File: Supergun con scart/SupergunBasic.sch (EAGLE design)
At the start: 37 parts, among them J1 AUDIO_JACK_3.5MM_PTH, X2 SCART-F

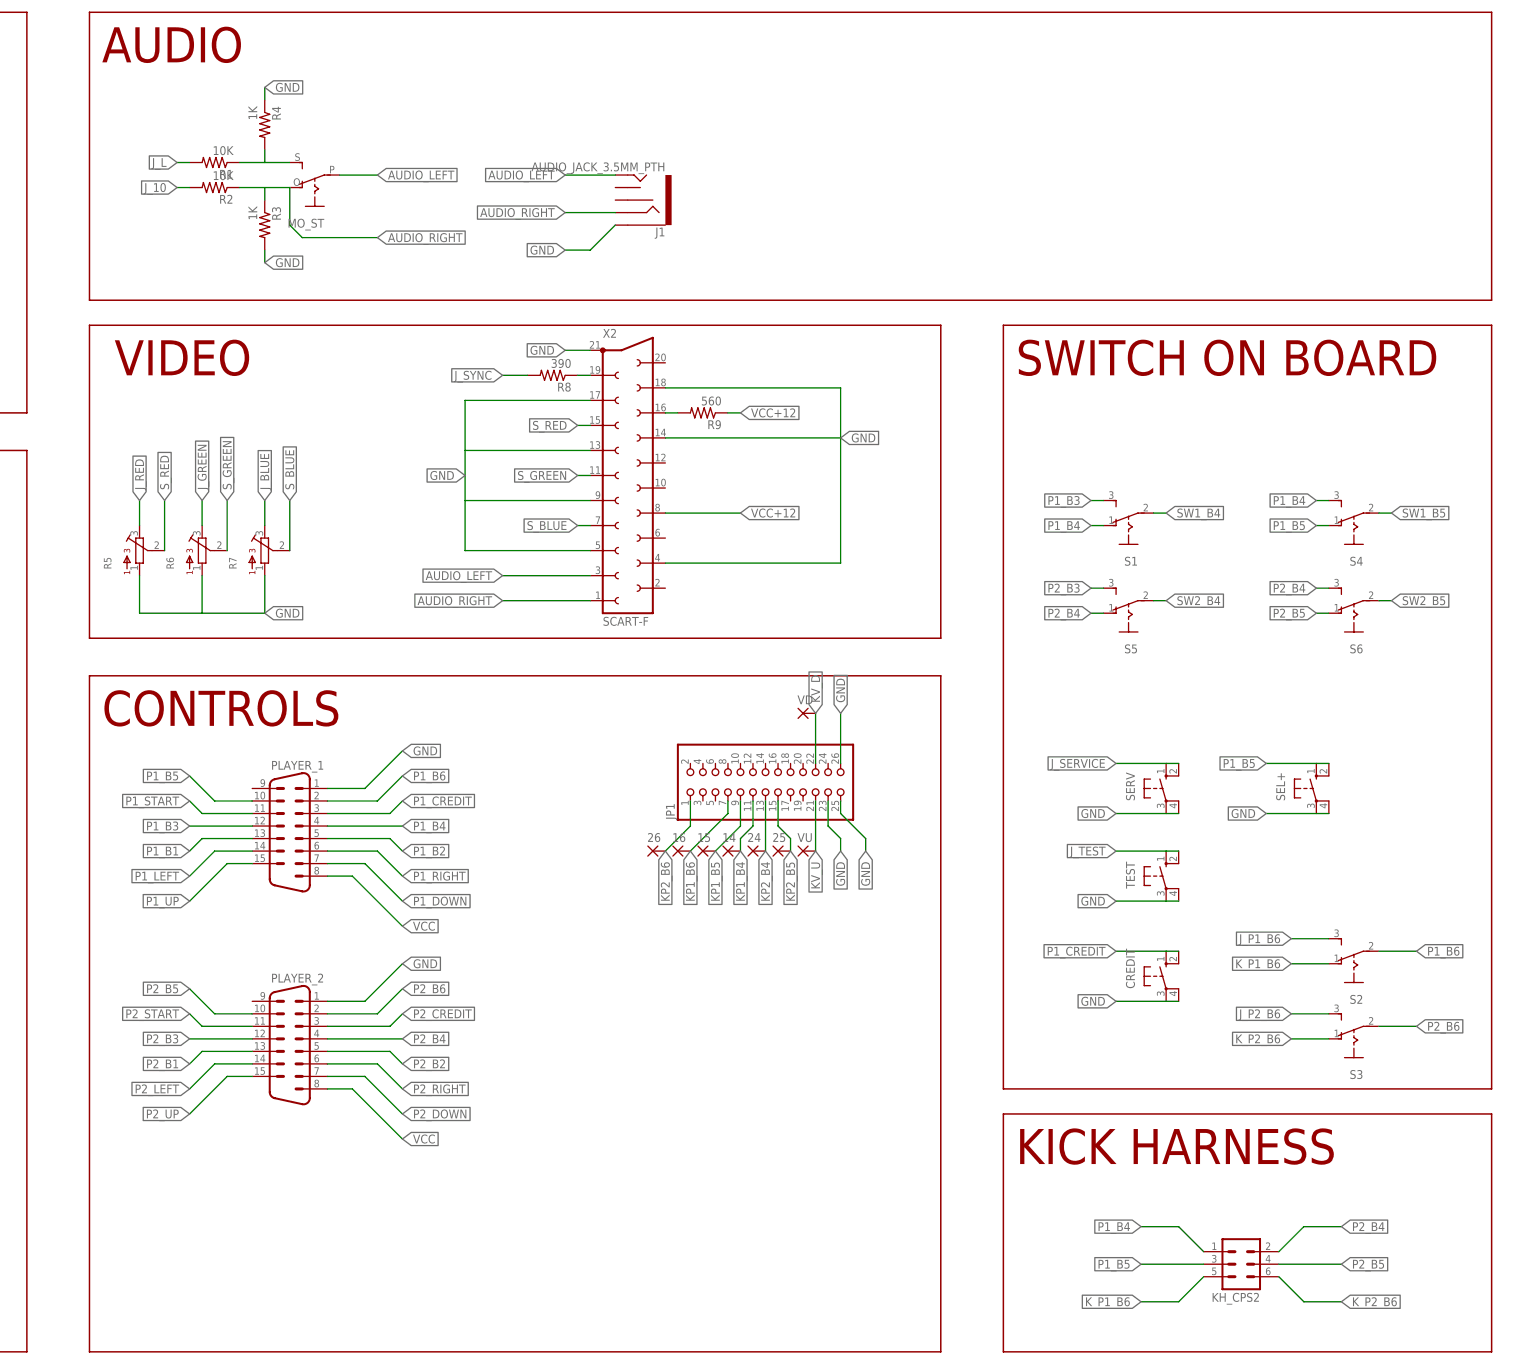
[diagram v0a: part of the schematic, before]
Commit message: Add files via upload
Actualizados sch y brd.

En el esquema se han icluïdo 2 subplacas que tienen que cortarse. Estas subplacas permiten conectarse al Kick Harness de CPS2. La pequeña va conectada a la Supergun (simplemente hacer coincidir los 2 circulos dibujados en una esquita del pinheader) y el grande va al connector Kick Harness de CPS2. Este incluye Vol+ y Vol- pero la supergun no se ha dado compatibilidad, por lo tanto estan para poder cablearos a unos swtich externos. Para usarlo simplemente asegurarse que el pin que señala la flecha es el de abajo la derecha al enchufarlo.
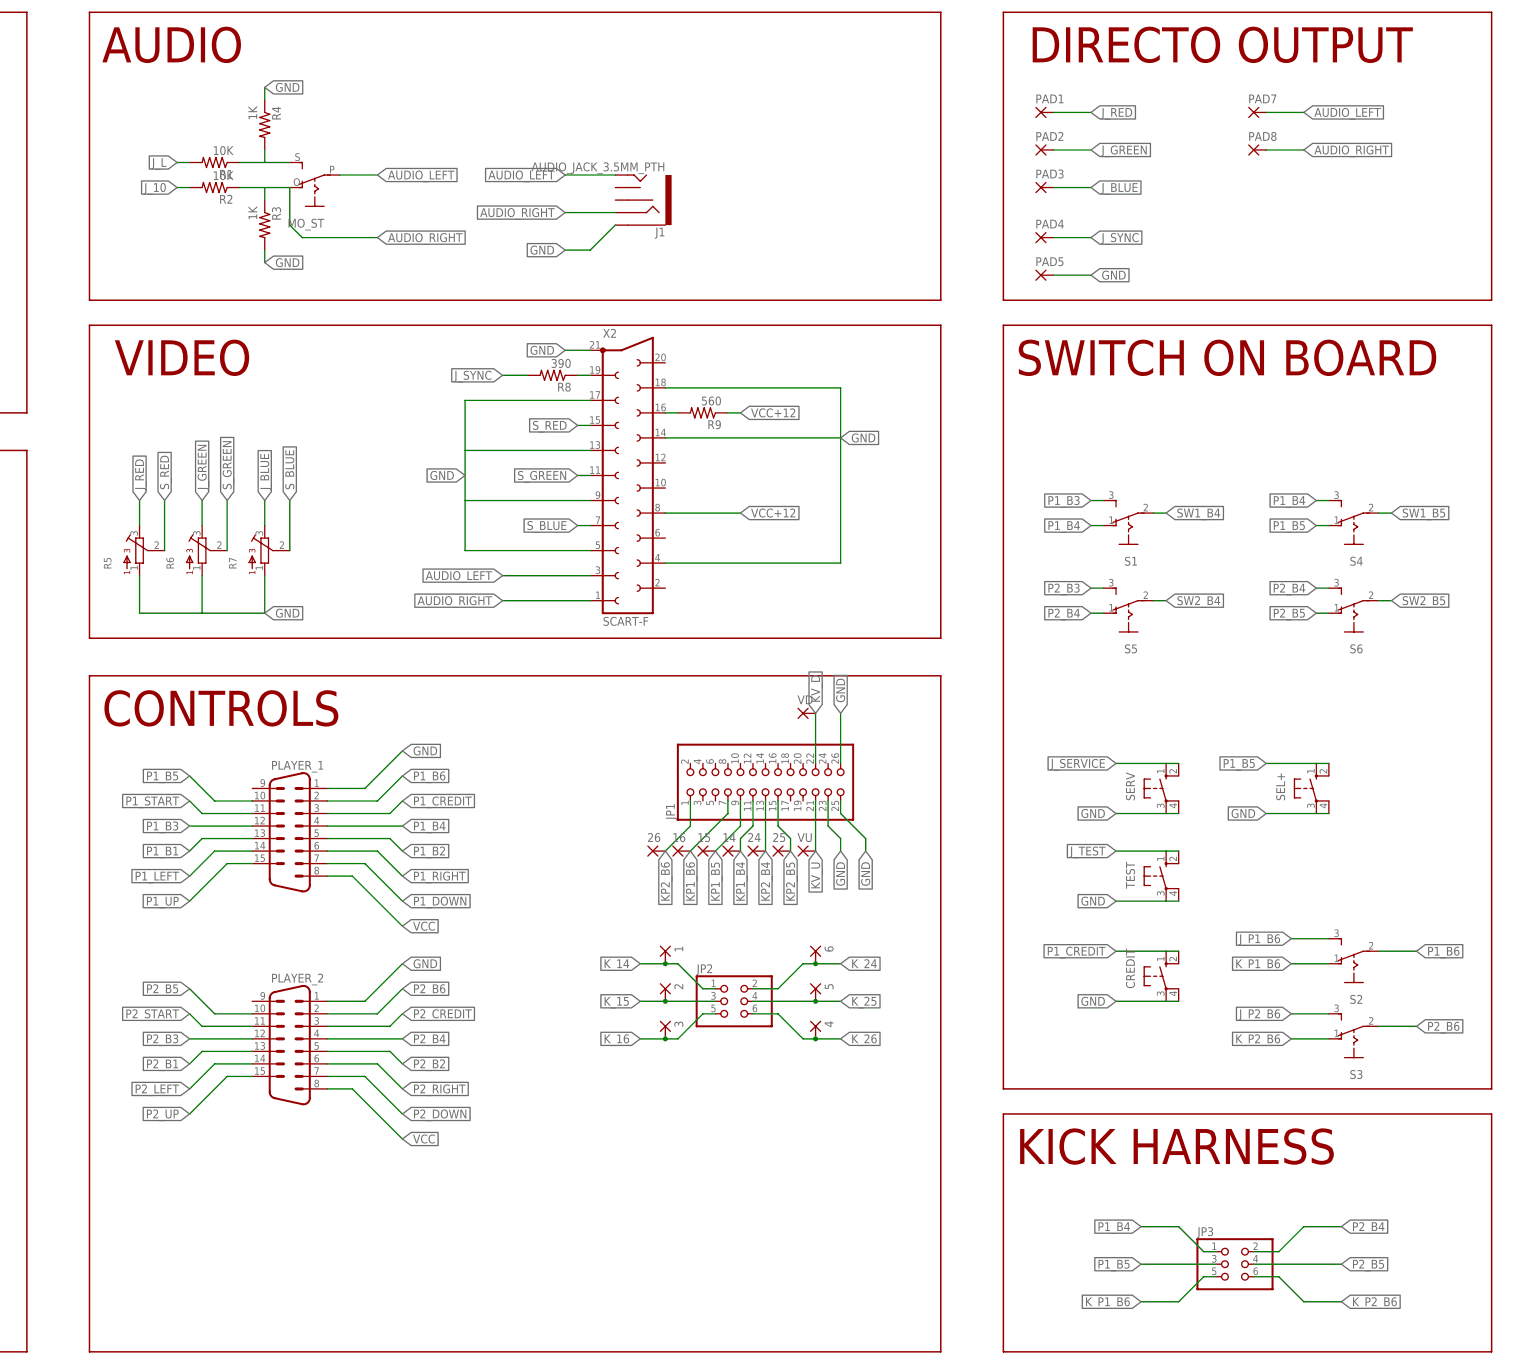
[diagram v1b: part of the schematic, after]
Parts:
- removed KH_CPS2: (no value), con-lstb:MA03-2
- added 1, 2, 3, 4, 5, 6, PAD1, PAD2, PAD3, PAD4, PAD5, PAD7, PAD8: (no value), wirepad:SMD2
- added JP2, JP3: (no value), pinhead:PINHD-2X3
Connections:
- new net K_14: 1.P, JP2.1
- new net K_15: 2.P, JP2.3
- new net K_16: 3.P, JP2.5
- new net K_24: 6.P, JP2.2
- new net K_25: 5.P, JP2.4
- new net K_26: 4.P, JP2.6
- net AUDIO_LEFT: now also PAD7.P
- net AUDIO_RIGHT: now also PAD8.P
- net GND: now also PAD5.P
- net J_BLUE: now also PAD3.P
- net J_GREEN: now also PAD2.P
- net J_RED: now also PAD1.P
- net J_SYNC: now also PAD4.P
- net K_P1_B6: now also JP3.5; no longer KH_CPS2.5
- net K_P2_B6: now also JP3.6; no longer KH_CPS2.6
- net P1_B4: now also JP3.1; no longer KH_CPS2.1
- net P1_B5: now also JP3.3; no longer KH_CPS2.3
- net P2_B4: now also JP3.2; no longer KH_CPS2.2
- net P2_B5: now also JP3.4; no longer KH_CPS2.4
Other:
- note added: "DIRECTO OUTPUT"

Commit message: Add files via upload
Actualización
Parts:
- removed MO_ST: (no value), adafruit:EG1218S
- removed PAD1, PAD2, PAD3, PAD4, PAD5, PAD7, PAD8: (no value), wirepad:SMD2
- removed S2, S3, S5, S6: (no value), switch:255SB
- removed X2: SCART-F, con-hirschmann:SCART-F
- added AUDIO, SYNC_G: (no value), con-wago-500:W237-102
- added JP4: (no value), pinhead:PINHD-1X3
- added R10: (no value), bourns:3362P
- added RGB: (no value), con-wago-500:W237-103
- added S10, S11, S12, S8, S9: (no value), SparkFun-Switches:SWITCH-SPDT-PTH-11.6X4.0MM
- added U$1: SCART_F, scart:SCART_F
- S1, S4: device switch:255SB -> SparkFun-Switches:SWITCH-SPDT-PTH-11.6X4.0MM
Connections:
- removed net N$1: R8.1, X2.19
- removed net N$11: JAMMA1.AUDIO+
- removed net N$3: MO_ST.S, R1.1, R4.2
- removed net N$4: R9.2, X2.16
- removed net N$5: JAMMA2.AUDIO_GND
- removed net P1_B6: PLAYER_1.2, S2.P
- removed net P2_B6: PLAYER_2.2, S3.P
- new net DIRECT_SYNC: JP4.2, SYNC_G-1.KL
- new net P_SYNC: JP4.3, R10.2, R8.2
- new net SCART_FAST_SW: R9.2, U$1.16
- new net SCART_SYNC: R8.1, U$1.19
- new net STR_LEFT: R1.1, R4.2, S8.S
- new net SW1_B6: PLAYER_1.2, S1.P
- new net SW2_B6: PLAYER_2.2, S4.P
- net AUDIO_LEFT: now also AUDIO-1.KL, S8.P, U$1.3; no longer MO_ST.P, PAD7.P, X2.3
- net AUDIO_RIGHT: now also AUDIO-2.KL, S8.O, U$1.1; no longer MO_ST.O, PAD8.P, X2.1
- net GND: now also R10.1, SYNC_G-2.KL, U$1.13, U$1.14, U$1.17, U$1.18, U$1.21, U$1.4, U$1.5, U$1.9; no longer PAD5.P, X2.13, X2.14, X2.17, X2.18, X2.21, X2.4, X2.5, X2.9
- net J_BLUE: now also RGB-1.KL; no longer PAD3.P
- net J_GREEN: now also RGB-2.KL; no longer PAD2.P
- net J_P1_B6: now also S1.S; no longer S2.S
- net J_P2_B6: now also S4.S; no longer S3.S
- net J_RED: now also RGB-3.KL; no longer PAD1.P
- net J_SYNC: now also JP4.1, R10.3; no longer PAD4.P, R8.2
- net K_P1_B6: now also S1.O; no longer S2.O
- net K_P2_B6: now also S4.O; no longer S3.O
- net P1_B3: now also S9.S; no longer S1.S
- net P1_B4: now also S12.S, S9.O; no longer PLAYER_1.4, S1.O, S4.S
- net P1_B5: now also S12.O; no longer PLAYER_1.10, S4.O
- net P2_B3: now also S11.S; no longer S5.S
- net P2_B4: now also S10.S, S11.O; no longer PLAYER_2.4, S5.O, S6.S
- net P2_B5: now also S10.O; no longer PLAYER_2.10, S6.O
- net SW1_B4: now also PLAYER_1.4, S9.P; no longer S1.P
- net SW1_B5: now also PLAYER_1.10, S12.P; no longer S4.P
- net SW2_B4: now also PLAYER_2.4, S11.P; no longer S5.P
- net SW2_B5: now also PLAYER_2.10, S10.P; no longer S6.P
- net S_BLUE: now also U$1.7; no longer X2.7
- net S_GREEN: now also U$1.11; no longer X2.11
- net S_RED: now also U$1.15; no longer X2.15
- net VCC+12: now also U$1.8; no longer X2.8
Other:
- note added: "KICK HARNESS ADD ON"
- moved on the sheet: 1, 14, 15, 16, 2, 24, 25, 26, 3, 4, 5, 6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

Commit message: Add files via upload
Optional LM1881 to scart connector, now you can select between lm1881 or jamma sync

LED added

Other improvements
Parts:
- added C1, C2: 0.1uF, SparkFun-Capacitors:0.1UF-KIT-EZ-50V-20%
- added IC1: LM1881N, oldchips2:LM1881N
- added JP5: (no value), pinhead:PINHD-1X3
- added LED1: (no value), led:LEDLD260
- added R11: 680k, adafruit:R-US_0204/7
- R8: value 390 -> 220
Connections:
- new net A_LEFT_OUT: J1.TSH, U$1.3
- new net A_RIGHT_OUT: J1.RSH, U$1.1
- new net C_SYNC: IC1G$1.CSYNC, JP5.3
- new net N$2: LED1.A, R8.2
- new net N$4: C2.1, IC1G$1.RSET, R11.2
- new net N$5: C1.2, IC1G$1.VIDEO
- new net VSYNC: IC1G$1.VS
- net AUDIO_LEFT: no longer U$1.3
- net AUDIO_RIGHT: no longer U$1.1
- net GND: now also C2.2, IC1P.GND, LED1.C, R11.1
- net J_GREEN: now also C1.1
- net J_SYNC: now also JP5.1
- net P_SYNC: no longer R8.2
- net SCART_SYNC: now also JP5.2; no longer R8.1
- net VCC: now also IC1P.VCC, R8.1
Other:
- note added: "DIRECT OUTPUT"
- note added: "SYNC ON GREEN"
- note removed: "DIRECTO OUTPUT"
- moved on the sheet: R8

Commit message: Add files via upload
GND pad on the Kick Harness
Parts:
- added GND: (no value), wirepad:SMD2
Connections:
- net GND: now also GND.P
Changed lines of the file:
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@@
 <part name="R11" library="adafruit" deviceset="R-US_" device="0204/7" value="680k"/>
 <part name="JP5" library="pinhead" library_urn="urn:adsk.eagle:library:325" deviceset="PINHD-1X3" device="" package3d_urn="urn:adsk.eagle:package:22458/2"/>
+<part name="GND" library="wirepad" library_urn="urn:adsk.eagle:library:412" deviceset="SMD2" device="" package3d_urn="urn:adsk.eagle:package:30839/1"/>
 </parts>
 <sheets>
@@
 <attribute name="VALUE" x="146.05" y="91.44" size="1.778" layer="96"/>
 </instance>
+<instance part="GND" gate="1" x="218.44" y="10.16" smashed="yes">
+<attribute name="NAME" x="217.297" y="12.0142" size="1.778" layer="95"/>
+<attribute name="VALUE" x="217.297" y="6.858" size="1.778" layer="96"/>
+</instance>
 </instances>
 <busses>
@@
 <label x="53.34" y="149.86" size="1.778" layer="95" xref="yes"/>
 </segment>
+<segment>
+<pinref part="GND" gate="1" pin="P"/>
+<wire x1="220.98" y1="10.16" x2="223.52" y2="10.16" width="0.1524" layer="91"/>
+<wire x1="223.52" y1="10.16" x2="223.52" y2="7.62" width="0.1524" layer="91"/>
+</segment>
 </net>
